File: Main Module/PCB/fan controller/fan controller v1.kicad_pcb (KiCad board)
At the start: 2 copper layers, 40.6 x 21.9 mm, 52 parts, among them P1 AUX, P2 +12V Suppply, P3 Fan, P4 Fan, P5 Jumper, Q1 NPN, U1 Octo

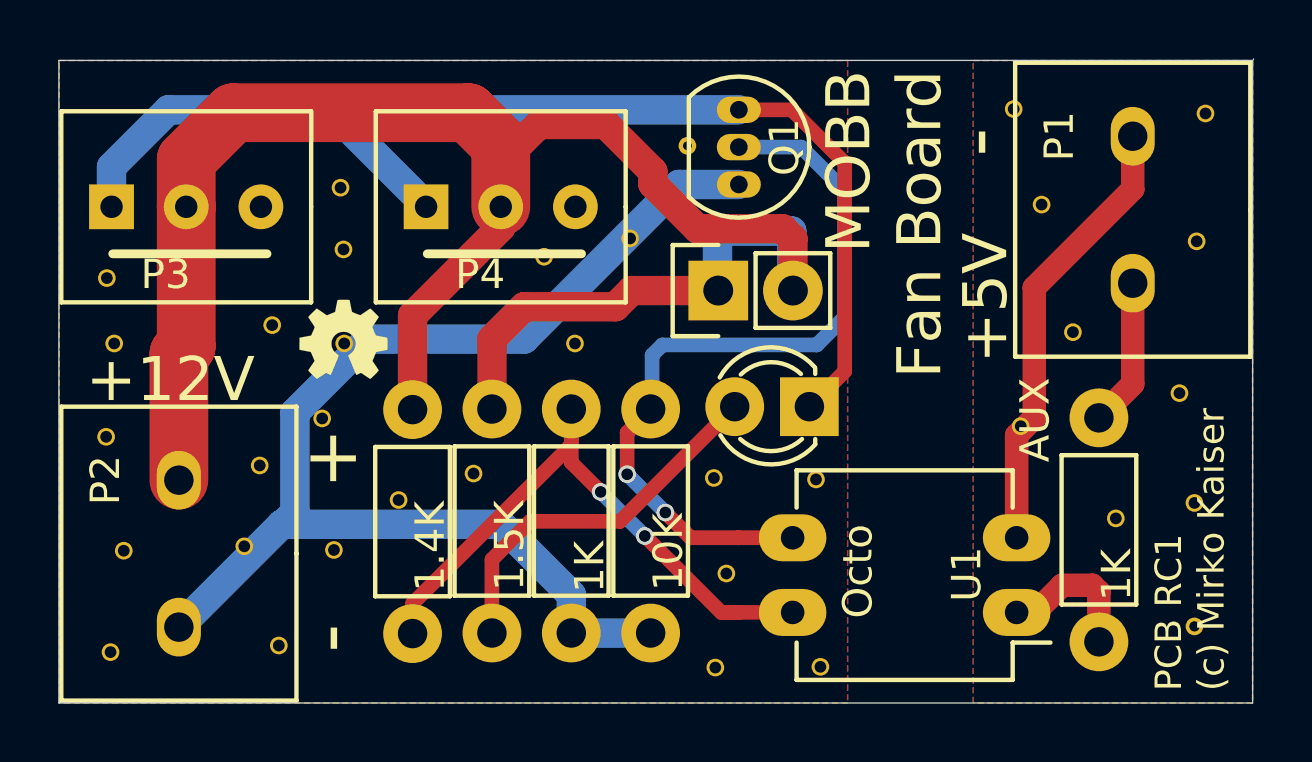
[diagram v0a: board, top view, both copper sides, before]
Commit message: * increased hole diameter and pad size for molex connector and screw terminals
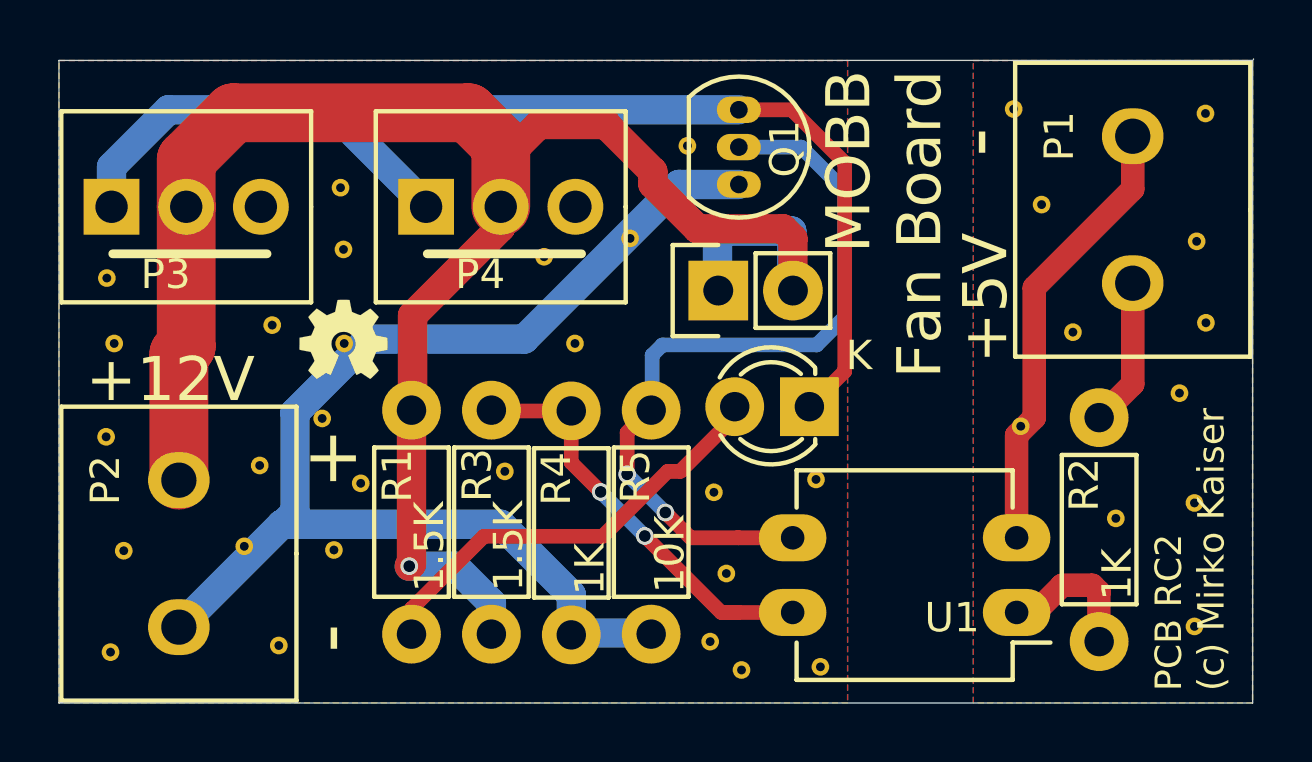
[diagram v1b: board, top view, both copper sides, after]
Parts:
- removed 1.4K, 1.5K, 10K, 1K: R, Resistors_ThroughHole:Resistor_Horizontal_RM7mm
- removed 1K: 1K, Resistors_ThroughHole:Resistor_Horizontal_RM7mm
- added R1: 1.5K, Resistors_ThroughHole:Resistor_Horizontal_RM7mm, F.Cu at (196.2, 140.5)
- added R2: 1K, Resistors_ThroughHole:Resistor_Horizontal_RM7mm, F.Cu at (219.6, 140.8)
- added R3: 1.5K, Resistors_ThroughHole:Resistor_Horizontal_RM7mm, F.Cu at (198.9, 140.5)
- added R4: 1K, Resistors_ThroughHole:Resistor_Horizontal_RM7mm, F.Cu at (201.6, 140.6)
- added R5: 10K, Resistors_ThroughHole:Resistor_Horizontal_RM7mm, F.Cu at (204.3, 140.5)
- U1: value Octo -> Ocot
- moved ? 5.22 mm to (223.2, 129.9)
- moved ? 1.41 mm to (194.4, 135.4)
- moved ? 1.07 mm to (199.3, 135.0)
- moved ? 0.89 mm to (207.4, 141.8)
- moved ? 0.74 mm to (206.3, 140.8)
- moved ? 0.49 mm to (206.5, 135.7)
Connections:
- P3 pad 3: Net-(P3-Pad3) -> (no net)
- P4 pad 3: Net-(P4-Pad3) -> (no net)
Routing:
- net Net-(R3-Pad2): track 21.8 -> 14.6 mm
- net Net-(D1-Pad2): track 12.9 -> 14.9 mm
- net +12V: track 66.1 -> 65.0 mm, vias 0 -> 1
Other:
- board text added: "PCB RC2 (c) Mirko Kaiser"
- board text removed: "PCB RC1 (c) Mirko Kaiser"
